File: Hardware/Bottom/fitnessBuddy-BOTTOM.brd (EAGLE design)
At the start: 33 x 33 mm, 47 parts, among them U4 PCF8523

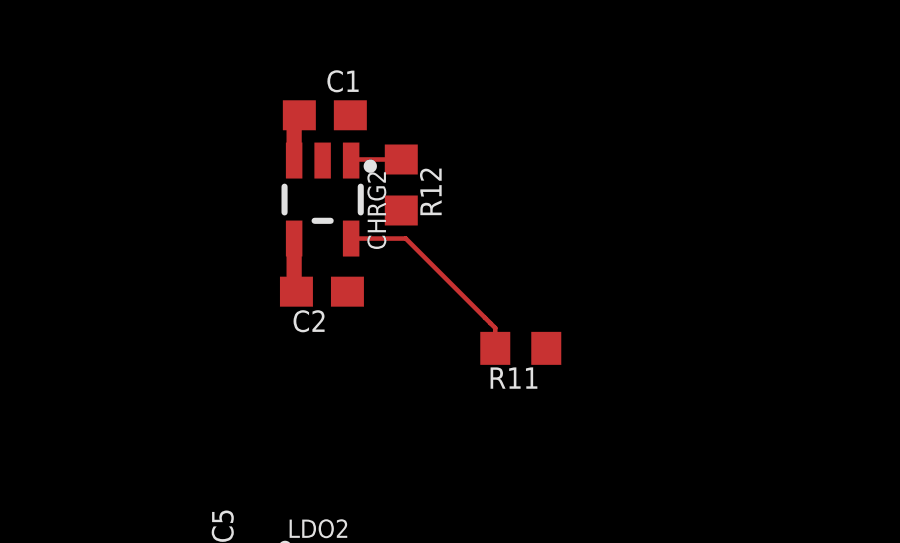
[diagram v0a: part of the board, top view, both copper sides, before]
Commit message: finished routing power management on top board
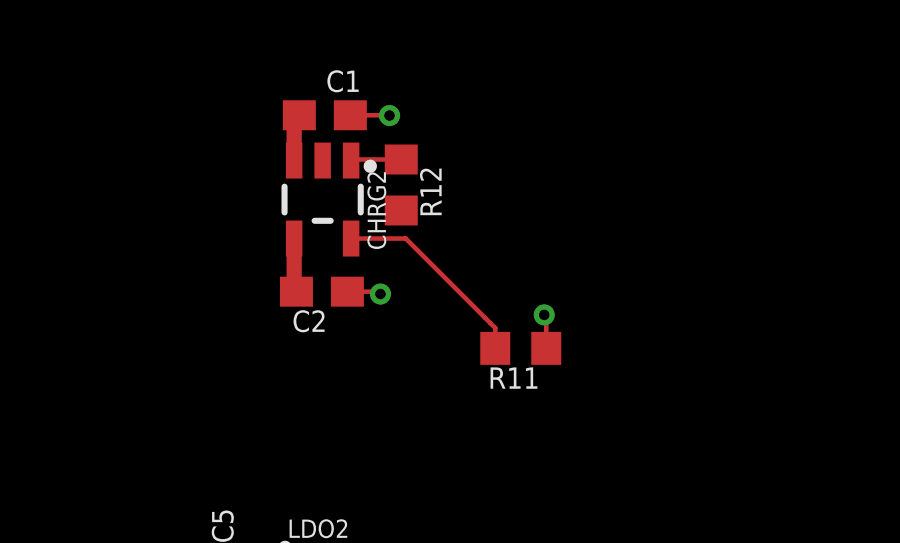
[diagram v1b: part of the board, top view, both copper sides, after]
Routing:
- net GND: track 35.9 -> 39.5 mm, vias 19 -> 22
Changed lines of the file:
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@@
 <wire x1="-23.468703125" y1="25.566" x2="-23.6448625" y2="25.389840625" width="0.1524" layer="1"/>
 <via x="-23.6448625" y="25.389840625" extent="1-16" drill="0.35"/>
+<wire x1="-18.5784625" y1="36.324540625" x2="-17.55648125" y2="36.324540625" width="0.1524" layer="1"/>
+<wire x1="-17.55648125" y1="36.324540625" x2="-17.477740625" y2="36.2458" width="0.1524" layer="1"/>
+<via x="-17.477740625" y="36.2458" extent="1-16" drill="0.35"/>
+<wire x1="-11.951603125" y1="34.434778125" x2="-11.951603125" y2="35.4821625" width="0.1524" layer="1"/>
+<wire x1="-11.951603125" y1="35.4821625" x2="-12.01928125" y2="35.549840625" width="0.1524" layer="1"/>
+<via x="-12.01928125" y="35.549840625" extent="1-16" drill="0.35"/>
+<wire x1="-18.48194375" y1="42.20464375" x2="-17.18564375" y2="42.20464375" width="0.1524" layer="1"/>
+<wire x1="-17.18564375" y1="42.20464375" x2="-17.17548125" y2="42.19448125" width="0.1524" layer="1"/>
+<via x="-17.17548125" y="42.19448125" extent="1-16" drill="0.35"/>
 <wire x1="23.817578125" y1="19.682225" x2="28.201625" y2="26.53448125" width="0" layer="19" extent="1-1"/>
 <wire x1="26.540459375" y1="16.514121875" x2="23.817578125" y2="19.682225" width="0" layer="19" extent="1-1"/>
@@
 <wire x1="15.577825" y1="5.768340625" x2="25.43301875" y2="5.87248125" width="0" layer="19" extent="1-1"/>
 <wire x1="6.76655625" y1="8.95768125" x2="13.92428125" y2="4.5821625" width="0" layer="19" extent="1-1"/>
-<wire x1="-14.201140625" y1="25.20188125" x2="4.74471875" y2="25.293321875" width="0" layer="19" extent="1-1"/>
-<wire x1="-20.8454" y1="26.2128" x2="-15.321284375" y2="25.466940625" width="0" layer="19" extent="1-1"/>
-<wire x1="-11.951603125" y1="34.434778125" x2="-15.308584375" y2="25.479640625" width="0" layer="19" extent="1-1"/>
-<wire x1="-18.5784625" y1="36.324540625" x2="-11.951603125" y2="34.434778125" width="0" layer="19" extent="1-1"/>
-<wire x1="-18.48194375" y1="42.20464375" x2="-18.5784625" y2="36.324540625" width="0" layer="19" extent="1-1"/>
-<wire x1="-19.405603125" y1="40.6955" x2="-18.48194375" y2="42.20464375" width="0" layer="19" extent="1-1"/>
-<wire x1="-15.24761875" y1="19.2405" x2="-15.308584375" y2="25.479640625" width="0" layer="19" extent="1-1"/>
+<wire x1="-11.951603125" y1="34.434778125" x2="4.75488125" y2="26.7335" width="0" layer="19" extent="1-1"/>
+<wire x1="-17.477740625" y1="36.2458" x2="-12.01928125" y2="35.549840625" width="0" layer="19" extent="1-1"/>
+<wire x1="-19.405603125" y1="40.6955" x2="-18.5784625" y2="36.324540625" width="0" layer="19" extent="1-1"/>
+<wire x1="-18.48194375" y1="42.20464375" x2="-19.405603125" y2="40.6955" width="0" layer="19" extent="1-1"/>
+<wire x1="-14.201140625" y1="25.20188125" x2="-11.951603125" y2="34.434778125" width="0" layer="19" extent="1-1"/>
+<wire x1="-20.8454" y1="26.2128" x2="-16.71828125" y2="25.466940625" width="0" layer="19" extent="1-1"/>
+<wire x1="-15.24761875" y1="19.2405" x2="-14.201140625" y2="25.20188125" width="0" layer="19" extent="1-1"/>
 <wire x1="-26.937478125" y1="17.0053" x2="-23.6448625" y2="25.389840625" width="0" layer="19" extent="1-1"/>
 </signal>

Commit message: organized top board
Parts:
- removed C1, C2: 4.7u, LinnesLab-Passives:C0603
- removed C5, C6: 1u, LinnesLab-Passives:C0603
- removed CHRG2: MCP73831, LinnesLab-Power:SOT23-5
- removed LDO2: MIC5504, LinnesLab-Power:SOT23-5
- removed R1, R12: 100k, LinnesLab-Passives:R0603
- removed R11: (no value), LinnesLab-Passives:R0603
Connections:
- removed net D27/CHRG.STATUS: CHRG2.1, R12.1
- removed net N$4: CHRG2.5, R11.2
- removed net VIN: C2.2, C5.2, CHRG2.4, LDO2.1, LDO2.3, R12.2
- removed net VLIPO: C1.1, CHRG2.3
- net 3.3V: no longer C6.1, LDO2.5, R1.2
- net GND: no longer C1.2, C2.1, C5.1, C6.2, CHRG2.2, LDO2.2, R1.1, R11.1
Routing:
- net GND: track 39.5 -> 30.1 mm, vias 22 -> 17
- net VIN: track 7.40 -> 0.00 mm
- net N$4: track 6.72 -> 0.00 mm
- net 3.3V: track 5.60 -> 1.32 mm, vias 1 -> 0
- net D27/CHRG.STATUS: track 1.69 -> 0.00 mm
- net VLIPO: track 1.58 -> 0.00 mm

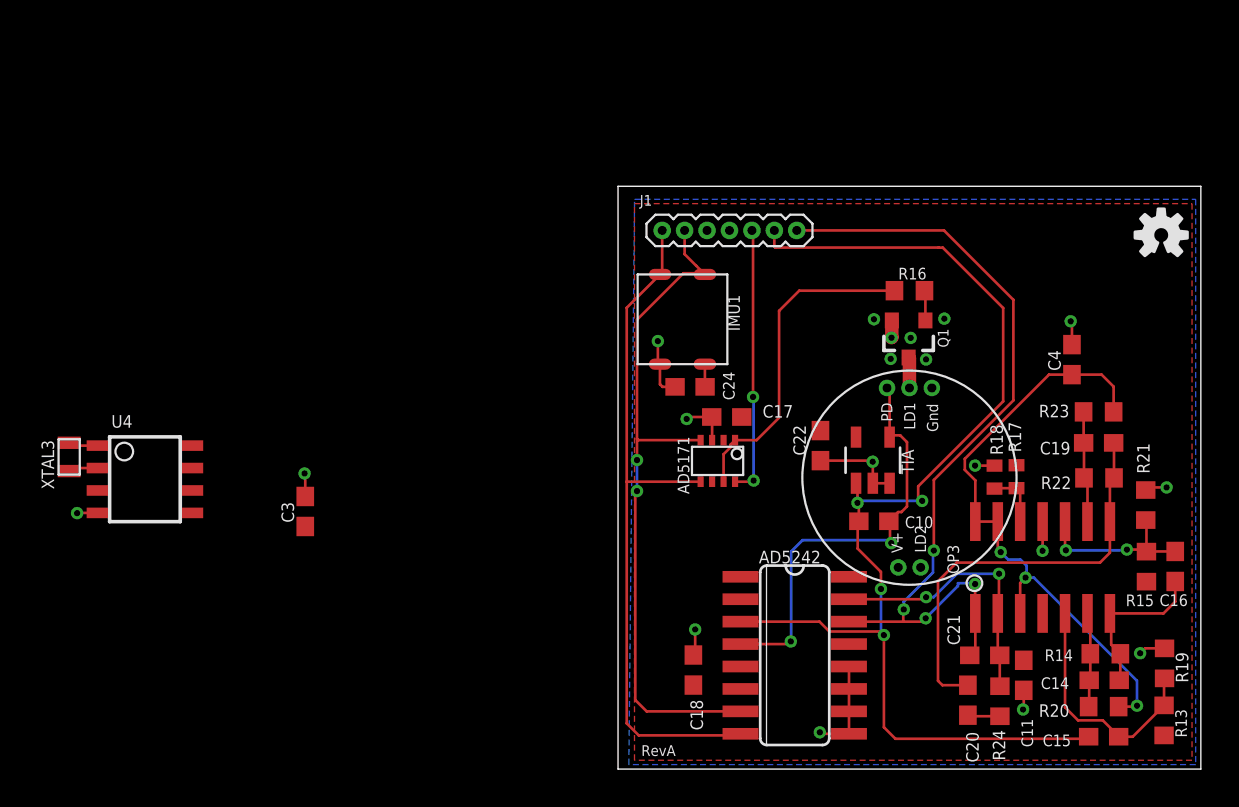
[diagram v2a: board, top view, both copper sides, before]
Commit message: reorganized bottom boards, added RTC to bottom board, and added notes to top schematic
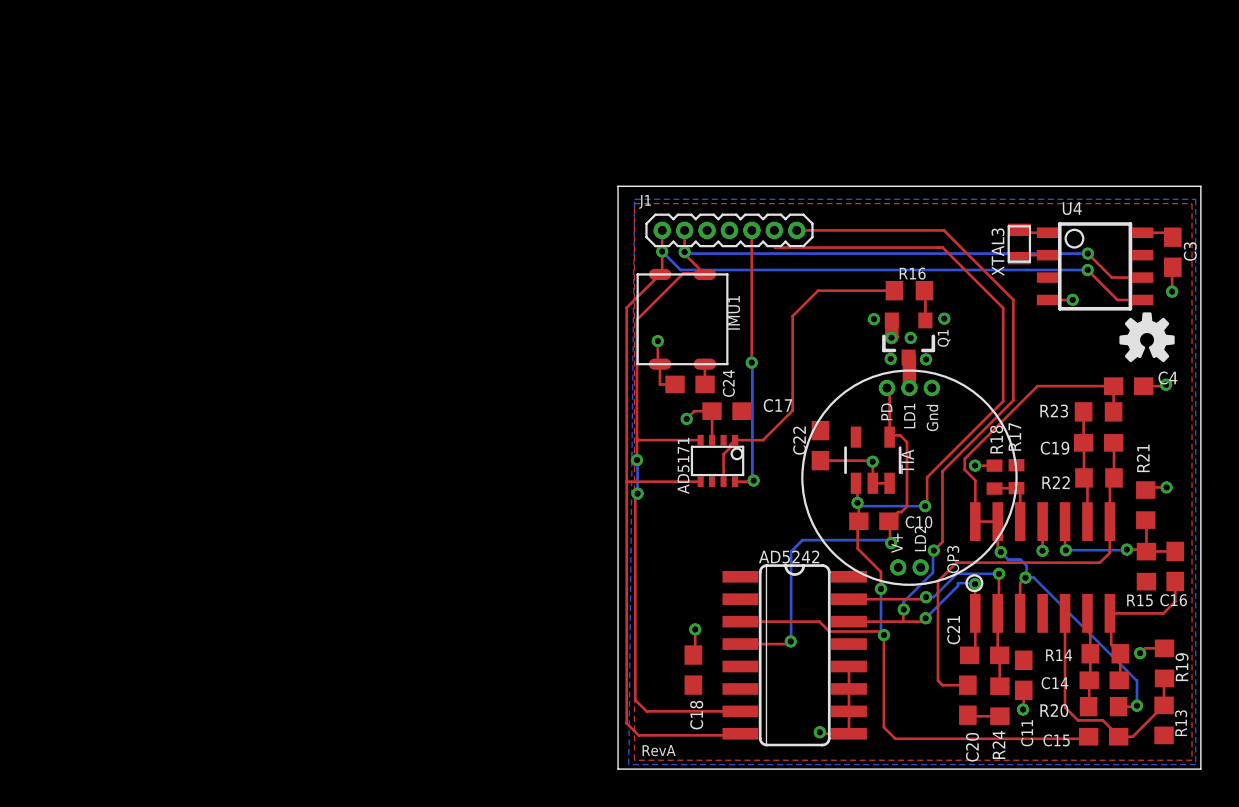
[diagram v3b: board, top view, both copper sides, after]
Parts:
- moved U4 55.1 mm to (29.5, 31.0)
- moved XTAL3 55.1 mm to (25.2, 32.2)
- moved C3 51.3 mm to (33.9, 31.8), turned to 270 degrees
- moved LOGO2 6.00 mm to (32.5, 26.8)
- moved C4 3.54 mm to (31.4, 24.2), turned to 0 degrees
- moved C17 0.33 mm to (8.67, 22.8)
- moved C24 0.14 mm to (6.58, 24.3)
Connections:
- net A7/PPG renamed A4/PPG
- net D29/LED.CTRL renamed D30/LED.CTRL
- new net A5/TIA: J1.6
- net A6/TIA: no longer J1.6
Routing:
- net SDA: track 39.7 -> 68.0 mm, vias 0 -> 2
- net SCL: track 39.3 -> 65.8 mm, vias 2 -> 4
- net 3.3V: track 1.32 -> 3.04 mm
- net VREF: track 35.1 -> 34.3 mm
- net A6/TIA: track 67.0 -> 66.3 mm
- net GND: track 30.1 -> 30.6 mm

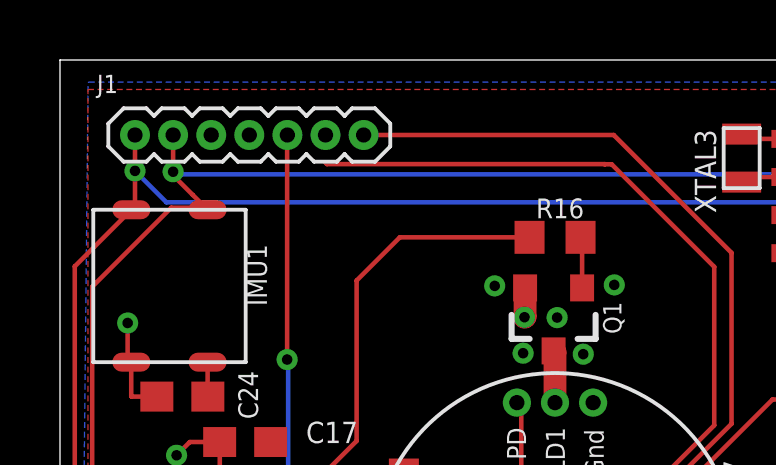
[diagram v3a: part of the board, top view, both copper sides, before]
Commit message: fixed pinout connecting bottom and top boards also added ppg module files
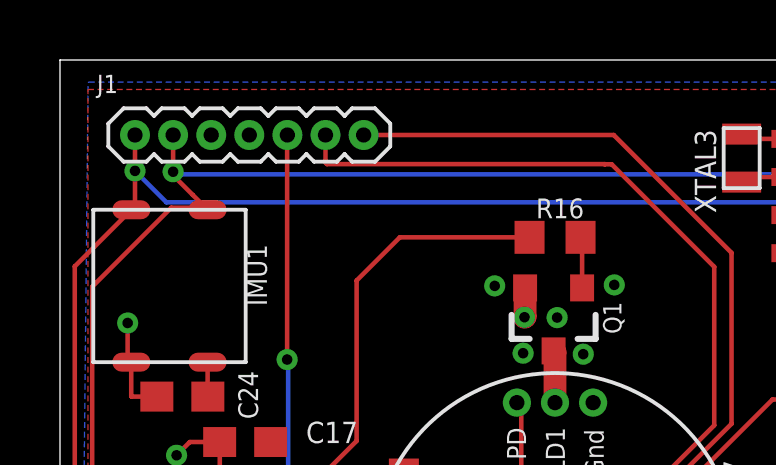
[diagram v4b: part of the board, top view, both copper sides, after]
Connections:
- removed net A6/TIA: AD5242.3, C10.2, C15.1, TIA.1
- net A5/TIA: now also AD5242.3, C10.2, C15.1, TIA.1
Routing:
- net A5/TIA: track 0.00 -> 67.2 mm, vias 0 -> 4
- net A6/TIA: track 66.3 -> 0.00 mm, vias 4 -> 0
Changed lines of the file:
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@@
 <?xml version="1.0" encoding="utf-8"?>
 <!DOCTYPE eagle SYSTEM "eagle.dtd">
-<eagle version="9.6.1">
+<eagle version="9.6.2">
 <drawing>
 <settings>
@@
 <layer number="17" name="Pads" color="2" fill="1" visible="yes" active="yes"/>
 <layer number="18" name="Vias" color="2" fill="1" visible="yes" active="yes"/>
-<layer number="19" name="Unrouted" color="6" fill="1" visible="no" active="yes"/>
+<layer number="19" name="Unrouted" color="6" fill="1" visible="yes" active="yes"/>
 <layer number="20" name="Dimension" color="24" fill="1" visible="yes" active="yes"/>
 <layer number="21" name="tPlace" color="7" fill="1" visible="yes" active="yes"/>
@@
 <via x="6.27" y="31.7754" extent="1-16" drill="0.35"/>
 </signal>
-<signal name="A6/TIA">
-<contactref element="C10" pad="2"/>
-<contactref element="AD5242" pad="3"/>
-<contactref element="C15" pad="1"/>
-<contactref element="TIA" pad="1"/>
-<wire x1="15.976565625" y1="18.683796875" x2="16.058778125" y2="18.601584375" width="0.1524" layer="1"/>
-<wire x1="16.058778125" y1="18.601584375" x2="16.058778125" y2="17.574259375" width="0.1524" layer="1"/>
-<wire x1="16.058778125" y1="17.574259375" x2="16.134978125" y2="17.498059375" width="0.1524" layer="1"/>
-<wire x1="16.134978125" y1="17.498059375" x2="16.134978125" y2="16.532859375" width="0.1524" layer="1"/>
-<wire x1="16.134978125" y1="16.532859375" x2="16.068940625" y2="16.466821875" width="0.1524" layer="1"/>
-<wire x1="16.068940625" y1="16.466821875" x2="16.068940625" y2="14.9823" width="0.1524" layer="1"/>
-<wire x1="17.3863" y1="13.664940625" x2="17.3863" y2="12.699740625" width="0.1524" layer="1"/>
-<wire x1="17.3863" y1="13.664940625" x2="16.068940625" y2="14.9823" width="0.1524" layer="1"/>
-<via x="17.3863" y="12.699740625" extent="1-16" drill="0.35"/>
-<wire x1="17.3863" y1="12.699740625" x2="17.3863" y2="10.256521875" width="0.1524" layer="16"/>
-<wire x1="17.3863" y1="10.256521875" x2="17.553940625" y2="10.08888125" width="0.1524" layer="16"/>
-<via x="17.553940625" y="10.08888125" extent="1-16" drill="0.35"/>
-<wire x1="17.553940625" y1="10.08888125" x2="17.553940625" y2="4.866640625" width="0.1524" layer="1"/>
-<wire x1="17.553940625" y1="4.866640625" x2="18.20418125" y2="4.2164" width="0.1524" layer="1"/>
-<wire x1="18.20418125" y1="4.2164" x2="29.030559375" y2="4.2164" width="0.1524" layer="1"/>
-<wire x1="29.030559375" y1="4.2164" x2="29.147396875" y2="4.3332375" width="0.1524" layer="1"/>
-<wire x1="9.431025" y1="10.848340625" x2="13.908340625" y2="10.848340625" width="0.1524" layer="1"/>
-<wire x1="13.908340625" y1="10.848340625" x2="14.4671375" y2="10.28954375" width="0.1524" layer="1"/>
-<wire x1="17.353278125" y1="10.28954375" x2="17.553940625" y2="10.08888125" width="0.1524" layer="1"/>
-<wire x1="14.4671375" y1="10.28954375" x2="17.353278125" y2="10.28954375" width="0.1524" layer="1"/>
-<wire x1="11.35" y1="32.078921875" x2="11.39951875" y2="32.029403125" width="0.1524" layer="1"/>
-<wire x1="11.39951875" y1="32.029403125" x2="20.665440625" y2="32.029403125" width="0.1524" layer="1"/>
-<wire x1="20.665440625" y1="32.029403125" x2="20.66035625" y2="32.02431875" width="0.1524" layer="1"/>
-<wire x1="20.66035625" y1="32.02431875" x2="20.8889625" y2="32.02431875" width="0.1524" layer="1"/>
-<wire x1="20.8889625" y1="32.02431875" x2="24.3078" y2="28.60548125" width="0.1524" layer="1"/>
-<wire x1="24.3078" y1="28.60548125" x2="24.3078" y2="23.3222875" width="0.1524" layer="1"/>
-<wire x1="24.3078" y1="23.3222875" x2="20.002503125" y2="19.016990625" width="0.1524" layer="1"/>
-<wire x1="20.002503125" y1="19.016990625" x2="20.002503125" y2="17.383759375" width="0.1524" layer="1"/>
-<wire x1="19.8882" y1="17.383759375" x2="20.002503125" y2="17.383759375" width="0.1524" layer="1"/>
-<via x="19.8882" y="17.383759375" extent="1-16" drill="0.35"/>
-<wire x1="19.8882" y1="17.383759375" x2="16.249278125" y2="17.383759375" width="0.1524" layer="16"/>
-<wire x1="16.058778125" y1="17.574259375" x2="16.249278125" y2="17.383759375" width="0.1524" layer="16"/>
-<via x="16.058778125" y="17.574259375" extent="1-16" drill="0.35"/>
-</signal>
 <signal name="PD.C">
 <contactref element="U$3" pad="PD"/>
@@
 <signal name="A5/TIA">
 <contactref element="J1" pad="6"/>
+<contactref element="C10" pad="2"/>
+<contactref element="AD5242" pad="3"/>
+<contactref element="C15" pad="1"/>
+<contactref element="TIA" pad="1"/>
+<wire x1="15.976565625" y1="18.683796875" x2="16.058778125" y2="18.601584375" width="0.1524" layer="1"/>
+<wire x1="16.058778125" y1="18.601584375" x2="16.058778125" y2="17.574259375" width="0.1524" layer="1"/>
+<wire x1="16.058778125" y1="17.574259375" x2="16.134978125" y2="17.498059375" width="0.1524" layer="1"/>
+<wire x1="16.134978125" y1="17.498059375" x2="16.134978125" y2="16.532859375" width="0.1524" layer="1"/>
+<wire x1="16.134978125" y1="16.532859375" x2="16.068940625" y2="16.466821875" width="0.1524" layer="1"/>
+<wire x1="16.068940625" y1="16.466821875" x2="16.068940625" y2="14.9823" width="0.1524" layer="1"/>
+<wire x1="17.3863" y1="13.664940625" x2="17.3863" y2="12.699740625" width="0.1524" layer="1"/>
+<wire x1="17.3863" y1="13.664940625" x2="16.068940625" y2="14.9823" width="0.1524" layer="1"/>
+<via x="17.3863" y="12.699740625" extent="1-16" drill="0.35"/>
+<wire x1="17.3863" y1="12.699740625" x2="17.3863" y2="10.256521875" width="0.1524" layer="16"/>
+<wire x1="17.3863" y1="10.256521875" x2="17.553940625" y2="10.08888125" width="0.1524" layer="16"/>
+<via x="17.553940625" y="10.08888125" extent="1-16" drill="0.35"/>
+<wire x1="17.553940625" y1="10.08888125" x2="17.553940625" y2="4.866640625" width="0.1524" layer="1"/>
+<wire x1="17.553940625" y1="4.866640625" x2="18.20418125" y2="4.2164" width="0.1524" layer="1"/>
+<wire x1="18.20418125" y1="4.2164" x2="29.030559375" y2="4.2164" width="0.1524" layer="1"/>
+<wire x1="29.030559375" y1="4.2164" x2="29.147396875" y2="4.3332375" width="0.1524" layer="1"/>
+<wire x1="9.431025" y1="10.848340625" x2="13.908340625" y2="10.848340625" width="0.1524" layer="1"/>
+<wire x1="13.908340625" y1="10.848340625" x2="14.4671375" y2="10.28954375" width="0.1524" layer="1"/>
+<wire x1="17.353278125" y1="10.28954375" x2="17.553940625" y2="10.08888125" width="0.1524" layer="1"/>
+<wire x1="14.4671375" y1="10.28954375" x2="17.353278125" y2="10.28954375" width="0.1524" layer="1"/>
+<wire x1="11.39951875" y1="32.029403125" x2="11.35" y2="32.078921875" width="0.1524" layer="1"/>
+<wire x1="11.39951875" y1="32.029403125" x2="20.665440625" y2="32.029403125" width="0.1524" layer="1"/>
+<wire x1="20.665440625" y1="32.029403125" x2="20.66035625" y2="32.02431875" width="0.1524" layer="1"/>
+<wire x1="20.66035625" y1="32.02431875" x2="20.8889625" y2="32.02431875" width="0.1524" layer="1"/>
+<wire x1="20.8889625" y1="32.02431875" x2="24.3078" y2="28.60548125" width="0.1524" layer="1"/>
+<wire x1="24.3078" y1="28.60548125" x2="24.3078" y2="23.3222875" width="0.1524" layer="1"/>
+<wire x1="24.3078" y1="23.3222875" x2="20.002503125" y2="19.016990625" width="0.1524" layer="1"/>
+<wire x1="20.002503125" y1="19.016990625" x2="20.002503125" y2="17.383759375" width="0.1524" layer="1"/>
+<wire x1="19.8882" y1="17.383759375" x2="20.002503125" y2="17.383759375" width="0.1524" layer="1"/>
+<via x="19.8882" y="17.383759375" extent="1-16" drill="0.35"/>
+<wire x1="19.8882" y1="17.383759375" x2="16.249278125" y2="17.383759375" width="0.1524" layer="16"/>
+<wire x1="16.058778125" y1="17.574259375" x2="16.249278125" y2="17.383759375" width="0.1524" layer="16"/>
+<via x="16.058778125" y="17.574259375" extent="1-16" drill="0.35"/>
+<wire x1="11.35" y1="32.078921875" x2="11.35" y2="33" width="0.1524" layer="1"/>
 </signal>
 </signals>
